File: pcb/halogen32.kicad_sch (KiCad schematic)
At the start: 31 parts, among them J1 Conn_02x05_Odd_Even, J2 USB_C_Receptacle_USB2.0_16P, J3 Conn_01x04_Socket, J4 Conn_01x16_Pin, J5 Conn_01x12_Pin, SW1 SW_SPDT, SW2 SW_SPDT, U1 STM32F411CEUx, U2 AMS1117-3.3, Y1 16MHz

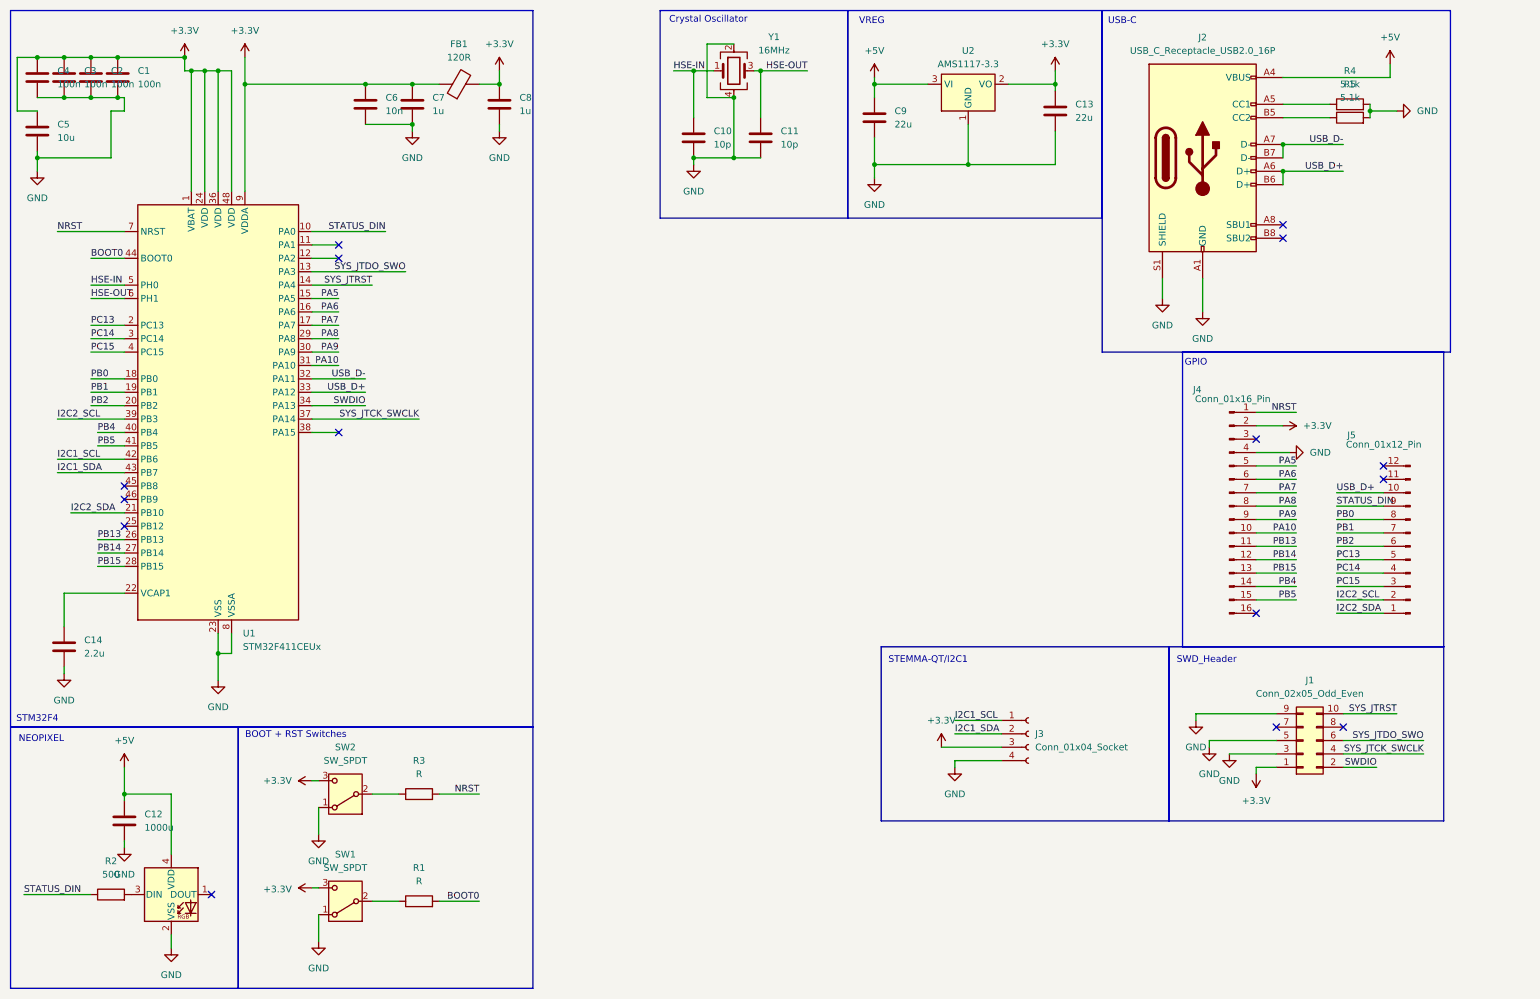
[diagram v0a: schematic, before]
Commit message: Moving schematic to Arduino Uno R4 form factor.
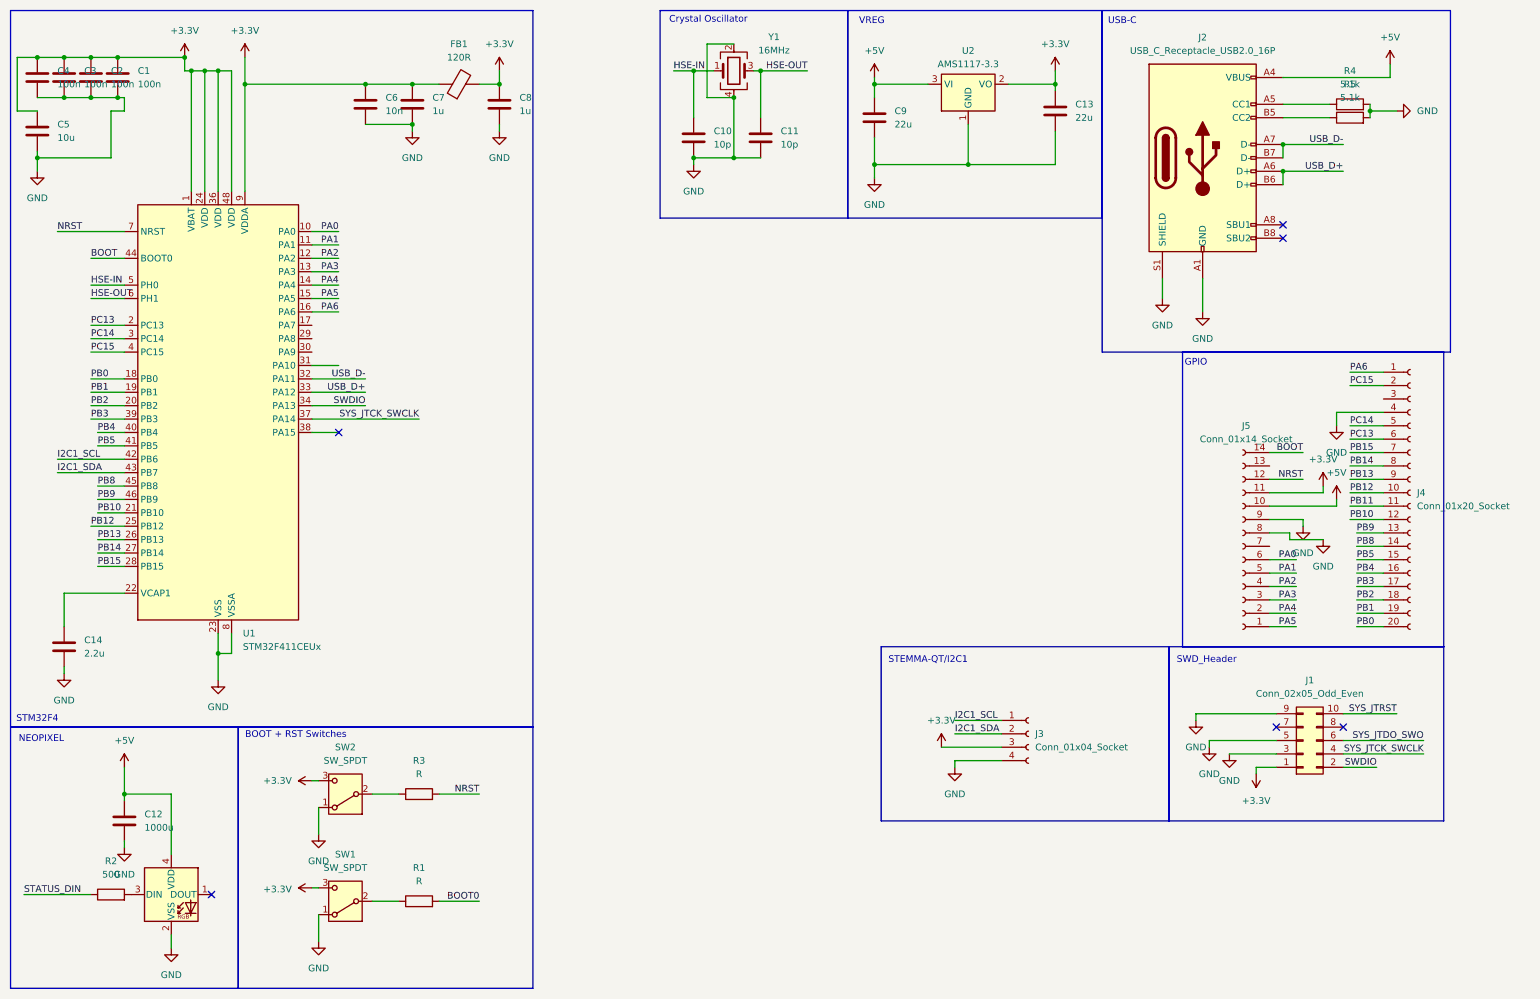
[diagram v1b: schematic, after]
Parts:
- removed J4: Conn_01x16_Pin, symbol Connector:Conn_01x16_Pin
- removed J5: Conn_01x12_Pin, symbol Connector:Conn_01x12_Pin
- added J4: Conn_01x20_Socket, symbol Connector:Conn_01x20_Socket
- added J5: Conn_01x14_Socket, symbol Connector:Conn_01x14_Socket
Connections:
- net +3.3V: now also J5.11 (Pin_11)
- net +5V: now also J5.10 (Pin_10)
- net BOOT0: no longer U1.44 (BOOT0)
- net GND: now also J4.4 (Pin_4), J5.8 (Pin_8), J5.9 (Pin_9)
- net NRST: now also J5.12 (Pin_12)
- net PA5: now also J5.1 (Pin_1)
- net PA6: now also J4.1 (Pin_1)
- net PB0: now also J4.20 (Pin_20)
- net PB1: now also J4.19 (Pin_19)
- net PB13: now also J4.9 (Pin_9)
- net PB14: now also J4.8 (Pin_8)
- net PB15: now also J4.7 (Pin_7)
- net PB2: now also J4.18 (Pin_18)
- net PB4: now also J4.16 (Pin_16)
- net PB5: now also J4.15 (Pin_15)
- net PC13: now also J4.6 (Pin_6)
- net PC14: now also J4.5 (Pin_5)
- net PC15: now also J4.2 (Pin_2)
- net STATUS_DIN: no longer U1.10 (PA0)
- net SYS_JTDO_SWO: no longer U1.13 (PA3)
- net SYS_JTRST: no longer U1.14 (PA4)
- net PA1: now reaches U1.11 (PA1)
- net PA1: now also J5.5 (Pin_5)
- net PA2: now reaches U1.12 (PA2)
- net PA2: now also J5.4 (Pin_4)
- net PB12: now reaches U1.25 (PB12)
- net PB12: now also J4.10 (Pin_10)
- net PB8: now reaches U1.45 (PB8)
- net PB8: now also J4.14 (Pin_14)
- net PB9: now reaches U1.46 (PB9)
- net PB9: now also J4.13 (Pin_13)
- net I2C2_SCL renamed PB3
- net PB3: now also J4.17 (Pin_17)
- net I2C2_SDA renamed PB10
- net PB10: now also J4.12 (Pin_12)
- net PA10: no longer names the net of U1.31 (PA10)
- net PA7: no longer names the net of U1.17 (PA7)
- net PA8: no longer names the net of U1.29 (PA8)
- net PA9: no longer names the net of U1.30 (PA9)
- new net BOOT: J5.14 (Pin_14), U1.44 (BOOT0)
- new net PA0: J5.6 (Pin_6), U1.10 (PA0)
- new net PA3: J5.3 (Pin_3), U1.13 (PA3)
- new net PA4: J5.2 (Pin_2), U1.14 (PA4)
- new net PB11: J4.11 (Pin_11)
- no-connect marks 15 -> 6

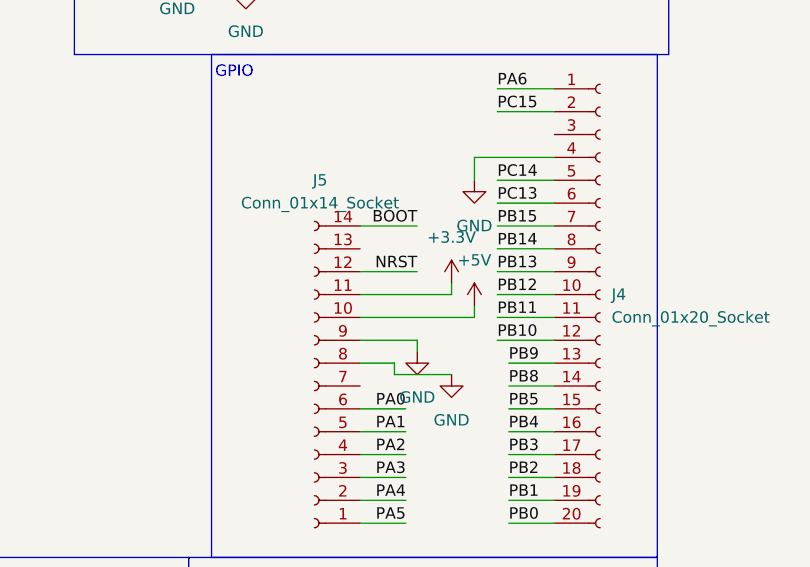
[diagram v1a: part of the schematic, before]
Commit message: Added IOREF pin and worked on shell.nix
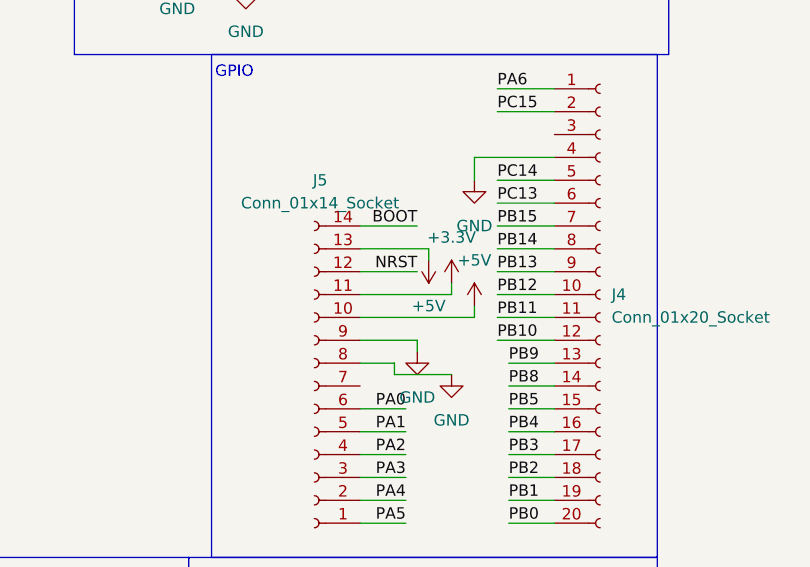
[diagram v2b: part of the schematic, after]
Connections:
- net +5V: now also J5.13 (Pin_13)
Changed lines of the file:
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@@
 	(wire
 		(pts
+			(xy 251.46 99.06) (xy 259.08 99.06)
+		)
+		(stroke
+			(width 0)
+			(type default)
+		)
+	)
+	(wire
+		(pts
 			(xy 105.41 24.13) (xy 105.41 26.67)
 		)
@@
 	(wire
 		(pts
+			(xy 259.08 100.33) (xy 259.08 99.06)
+		)
+		(stroke
+			(width 0)
+			(type default)
+		)
+	)
+	(wire
+		(pts
 			(xy 267.97 116.84) (xy 273.05 116.84)
 		)
@@
 					(unit 1)
 				)
+			)
+		)
+	)
+	(symbol
+		(lib_id "power:+5V")
+		(at 259.08 100.33 180)
+		(unit 1)
+		(exclude_from_sim no)
+		(in_bom yes)
+		(on_board yes)
+		(dnp no)
+		(fields_autoplaced yes)
+		(property "Reference" "#PWR035"
+			(at 259.08 96.52 0)
+			(effects
+				(font
+					(size 1.27 1.27)
+				)
+				(hide yes)
+			)
+		)
+		(property "Value" "+5V"
+			(at 259.08 105.41 0)
+			(effects
+				(font
+					(size 1.27 1.27)
+				)
+			)
+		)
+		(property "Footprint" ""
+			(at 259.08 100.33 0)
+			(effects
+				(font
+					(size 1.27 1.27)
+				)
+				(hide yes)
+			)
+		)
+		(property "Datasheet" ""
+			(at 259.08 100.33 0)
+			(effects
+				(font
+					(size 1.27 1.27)
+				)
+				(hide yes)
+			)
+		)
+		(property "Description" "Power symbol creates a global label with name \"+5V\""
+			(at 259.08 100.33 0)
+			(effects
+				(font
+					(size 1.27 1.27)
+				)
+				(hide yes)
+			)
+		)
+		(pin "1"
+		)
+		(instances
+			(project ""
+				(path "/0dddf3a6-05c9-4d23-8b33-d0c9438795f8"
+					(reference "#PWR035")
+					(unit 1)
+				)

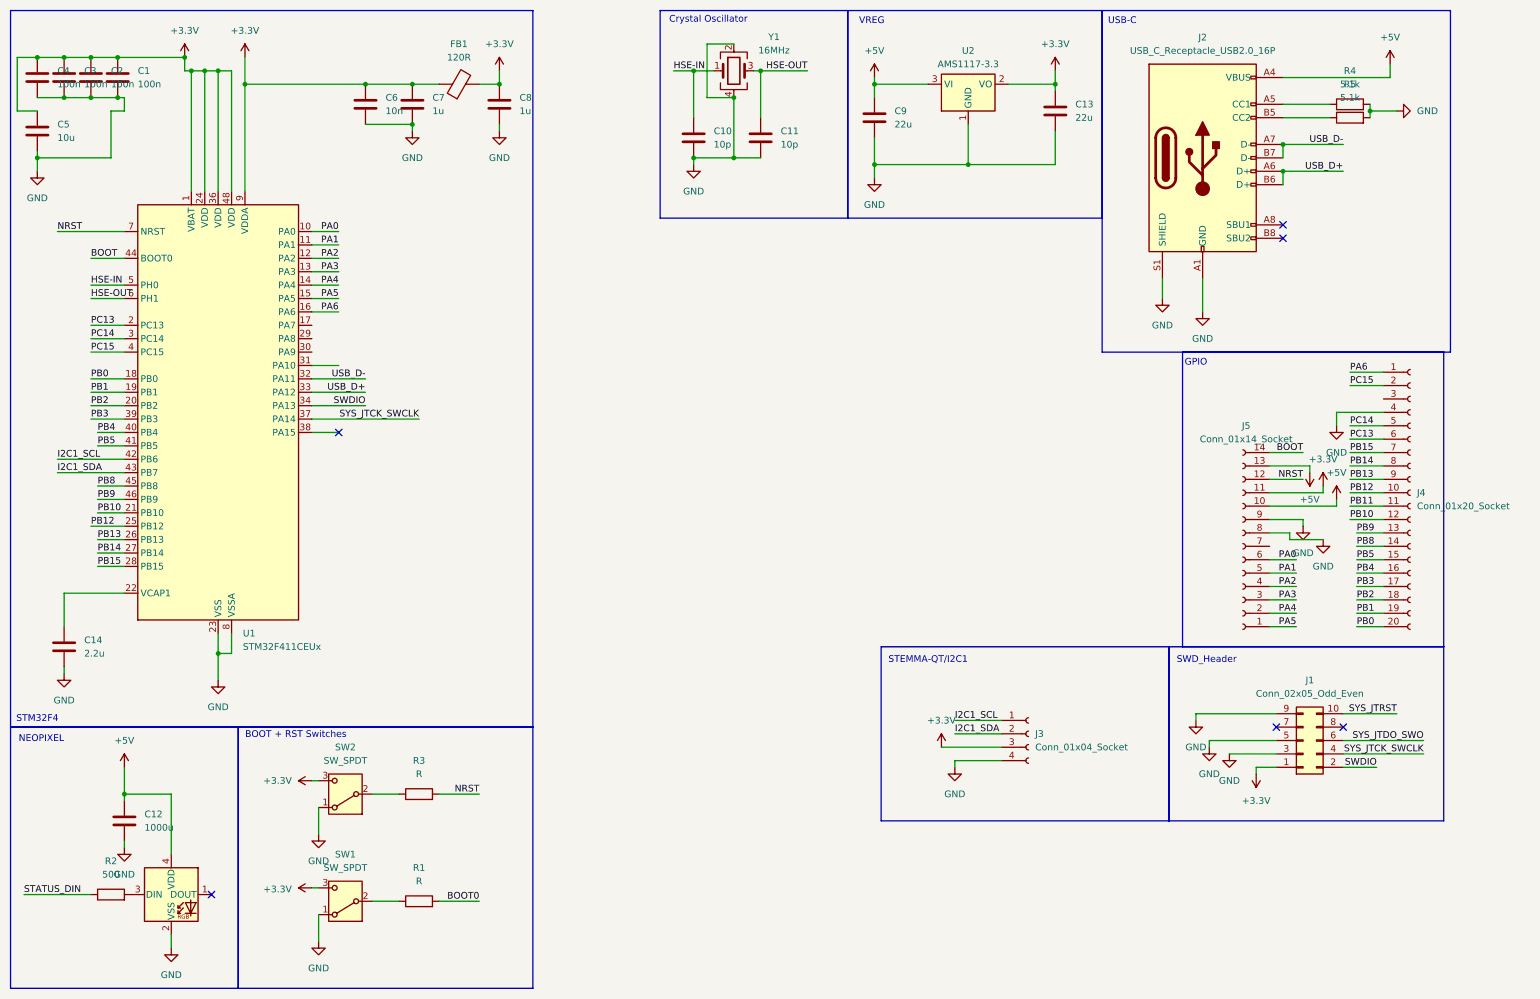
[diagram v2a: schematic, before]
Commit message: Added DC jack and buck converter
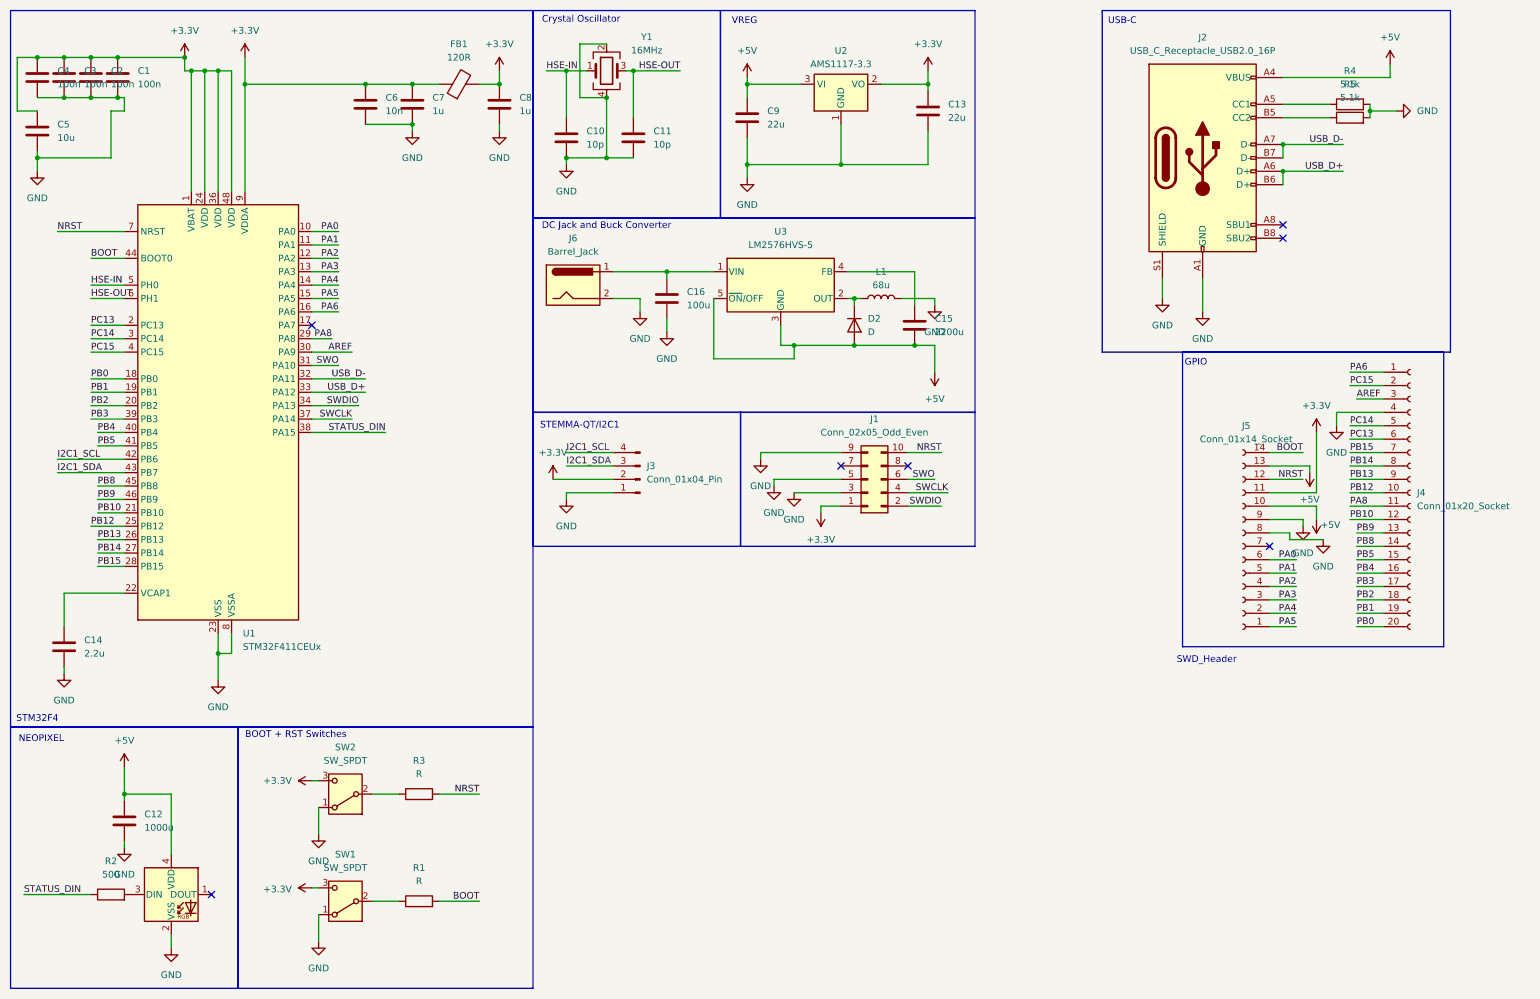
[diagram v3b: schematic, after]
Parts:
- removed J3: Conn_01x04_Socket, symbol Connector:Conn_01x04_Socket
- added C15: 2200u, symbol Device:C
- added C16: 100u, symbol Device:C
- added D2: D, symbol Device:D
- added J3: Conn_01x04_Pin, symbol Connector:Conn_01x04_Pin
- added J6: Barrel_Jack, symbol Connector:Barrel_Jack
- added L1: 68u, symbol Device:L
- added U3: LM2576HVS-5, Package_TO_SOT_SMD:TO-263-5_TabPin3, symbol Regulator_Switching:LM2576HVS-5
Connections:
- net BOOT0 is gone; now on net BOOT: R1.2
- net PB11 is gone; now on net PA8: J4.11 (Pin_11)
- net SYS_JTDO_SWO is gone; now on net SWO: J1.6 (Pin_6)
- net SYS_JTRST is gone; now on net NRST: J1.10 (Pin_10)
- net +3.3V: now also J3.2 (Pin_2)
- net +5V: now also C15.2, D2.2 (A), U3.3 (GND), U3.5 (~{ON}/OFF)
- net GND: now also C16.2, J3.1 (Pin_1), J6.2, L1.2
- net I2C1_SCL: now also J3.4 (Pin_4)
- net I2C1_SDA: now also J3.3 (Pin_3)
- net STATUS_DIN: now also U1.38 (PA15)
- net PA8: now reaches U1.29 (PA8)
- net AREF: now reaches U1.30 (PA9)
- net AREF: now also J4.3 (Pin_3)
- net SWO: now reaches U1.31 (PA10)
- net SYS_JTCK_SWCLK renamed SWCLK
- new net: C16.1, J6.1, U3.1 (VIN)
- new net: D2.1 (K), L1.1, U3.2 (OUT)
- new net: C15.1, U3.4 (FB)
- no-connect marks 6 -> 7
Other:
- note added: "DC Jack and Buck Converter"
- moved on the sheet: C10, C11, C13, C9, J1, U2, Y1
